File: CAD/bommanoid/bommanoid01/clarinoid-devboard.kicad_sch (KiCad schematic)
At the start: 144 parts, among them IC1 PCA9554APW,118, J1 AudioOut, J10 MIDI IN, J11 MIDI OUT, J12 SSD1306, J13 captouch 3x3x1 header B, J14 captouch4x4x2 headerA, J15 captouch4x4x2 header B, J16 captouch4x4x2, J17 captouch4x4x3 headerA, J18 captouch4x4x3 header B, J19 captouch4x4x.5 headerA, J2 XKB_U262-16XN-4BVC11 USB-C re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, J20 CapTouchSlider_3x3x1, J21 captouch4x4x.5 header B, J22 captouch4x4x3, J23 captouch4x4x.5, J24 captouch5x5x1 headerA, J25 captouch5x5x1 header B, J26 captouch4x4x1 headerA, J27 captouch4x4x1 header B, J28 captouch5x5x1, J29 captouch4x4x1, J31 4p, J32 header_power tap, J43 Conn_01x20, J44 Conn_01x08, J45 female 1x6, J5 header_i2c, J52 female 1x6, J53 female 1x6, J6 female 1x6, J8 female 1x4, J9 captouch 3x3x1 headerA, SW2 SW_Push, SW3 SW_Push, SW4 SW_Push, SW5 SW_Push, SW7 RotaryEncoder_Switch_ABC12, U1 PCM5102A, U10 captouch4x4x2 graphic, U11 captouch4x4x3 graphic, U12 ssd1306_graphic, U13 captouch4x4x.5 graphic, U14 captouch5x5x1 graphic, U15 captouch4x4x1 graphic, U16 power template, U20 mb1, U21 mb1, U22 mb1, U23 mb1, U24 mb1, U25 mb1, U26 mb1, U27 mb1, U28 mb1, U29 mb1, U30 mb1, U31 mb1, U32 mb1, U33 mb1, U34 mb1, U35 mb1, U36 mb1, U37 mb1, U38 WS2812, U4 captouch board template, U44 processor board template, U48 mb1, U49 mb1, U50 mb1, U51 mb1, U52 mb1, U53 mb1, U54 mb1, U55 mb1, U56 mb1, U57 mb1, U58 mb1, U59 mb1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

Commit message: bomma design progress
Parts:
- removed C10, C11, C3, C5: 10uF, Capacitor_SMD:C_0805_2012Metric, symbol Device:C
- removed C12, C7, C8, C9: 2.2uF, Capacitor_SMD:C_0805_2012Metric, symbol Device:C
- removed C13, C14, C23, C27, C4, C6: 0.1uF, Capacitor_SMD:C_0805_2012Metric, symbol Device:C
- removed C17, C20, C21, C22: 22uF, Capacitor_SMD:C_0805_2012Metric, symbol Device:C
- removed D5, D7: blue, LED_SMD:LED_0603_1608Metric, symbol Device:LED
- removed D6: 1N4148WS, Diode_SMD:D_SOD-323, symbol Device:D
- removed D8, D9: green, LED_SMD:LED_0603_1608Metric, symbol Device:LED
- removed H1: MountingHole, clarinoid2:MountingHole_3.2mm_M3_Pad_SQUARE, symbol Mechanical:MountingHole_Pad
- removed H13, H14, H15: MountingHole, MountingHole:MountingHole_3.2mm_M3, symbol Mechanical:MountingHole
- removed H2, H3, H5: MountingHole, MountingHole:MountingHole_3.2mm_M3_Pad_Via, symbol Mechanical:MountingHole_Pad
- removed IC1: PCA9554APW,118, SamacSys_Parts:SOP65P640X110-16N, symbol SamacSys_Parts:PCA9554APW,118
- removed J1: AudioOut, clarinoid2:SWITCHCRAFT_35RAPC4BV4_OvalHoles, symbol clarinoid2:Switchcraft 35RAPC4BV4
- removed J10: MIDI IN, clarinoid2:SWITCHCRAFT_35RAPC4BV4_OvalHoles, symbol clarinoid2:Switchcraft 35RAPC4BV4
- removed J11: MIDI OUT, clarinoid2:SWITCHCRAFT_35RAPC4BV4_OvalHoles, symbol clarinoid2:Switchcraft 35RAPC4BV4
- removed J12: SSD1306, Connector_PinSocket_2.54mm:PinSocket_1x07_P2.54mm_Vertical, symbol clarinoid2:SSD1306
- removed J13: captouch 3x3x1 header B, Connector_PinHeader_2.54mm:PinHeader_1x06_P2.54mm_Vertical, symbol Connector_Generic:Conn_01x06
- removed J14: captouch4x4x2 headerA, Connector_PinHeader_2.54mm:PinHeader_1x06_P2.54mm_Vertical, symbol Connector_Generic:Conn_01x06
- removed J15: captouch4x4x2 header B, Connector_PinHeader_2.54mm:PinHeader_1x06_P2.54mm_Vertical, symbol Connector_Generic:Conn_01x06
- removed J16: captouch4x4x2, CapTouchSliders:CaptouchSlider_Masked_H4x4_A2.0mm_x12, symbol Connector_Generic:Conn_01x12
- removed J17: captouch4x4x3 headerA, Connector_PinHeader_2.54mm:PinHeader_1x06_P2.54mm_Vertical, symbol Connector_Generic:Conn_01x06
- removed J18: captouch4x4x3 header B, Connector_PinHeader_2.54mm:PinHeader_1x06_P2.54mm_Vertical, symbol Connector_Generic:Conn_01x06
- removed J19: captouch4x4x.5 headerA, Connector_PinHeader_2.54mm:PinHeader_1x06_P2.54mm_Vertical, symbol Connector_Generic:Conn_01x06
- removed J2: XKB_U262-16XN-4BVC11 USB-C recept, clarinoid2:USB_C_Receptacle_XKB_U262-16XN-4BVC11, symbol clarinoid2:USB_C_Plug_USB2.0
- removed J20: CapTouchSlider_3x3x1, CapTouchSliders:CaptouchSlider_Masked_H3x3_A1.0mm_x12, symbol Connector_Generic:Conn_01x12
- removed J21: captouch4x4x.5 header B, Connector_PinHeader_2.54mm:PinHeader_1x06_P2.54mm_Vertical, symbol Connector_Generic:Conn_01x06
- removed J22: captouch4x4x3, CapTouchSliders:CaptouchSlider_Masked_H4x4_A3.0mm_x12, symbol Connector_Generic:Conn_01x12
- removed J23: captouch4x4x.5, CapTouchSliders:CaptouchSlider_Masked_H4x4_A0.5mm_x12, symbol Connector_Generic:Conn_01x12
- removed J24: captouch5x5x1 headerA, Connector_PinHeader_2.54mm:PinHeader_1x06_P2.54mm_Vertical, symbol Connector_Generic:Conn_01x06
- removed J25: captouch5x5x1 header B, Connector_PinHeader_2.54mm:PinHeader_1x06_P2.54mm_Vertical, symbol Connector_Generic:Conn_01x06
- removed J26: captouch4x4x1 headerA, Connector_PinHeader_2.54mm:PinHeader_1x06_P2.54mm_Vertical, symbol Connector_Generic:Conn_01x06
- removed J27: captouch4x4x1 header B, Connector_PinHeader_2.54mm:PinHeader_1x06_P2.54mm_Vertical, symbol Connector_Generic:Conn_01x06
- removed J28: captouch5x5x1, CapTouchSliders:CaptouchSlider_Masked_H5x5_A1.0mm_x12, symbol Connector_Generic:Conn_01x12
- removed J29: captouch4x4x1, CapTouchSliders:CaptouchSlider_Masked_H4x4_A1.0mm_x12, symbol Connector_Generic:Conn_01x12
- removed J31: 4p, Connector_PinSocket_2.54mm:PinSocket_1x04_P2.54mm_Vertical, symbol Connector_Generic:Conn_01x04
- removed J32: header_power tap, Connector_PinSocket_2.54mm:PinSocket_1x02_P2.54mm_Vertical, symbol Connector_Generic:Conn_01x02
- removed J43: Conn_01x20, Connector_PinSocket_2.54mm:PinSocket_1x20_P2.54mm_Vertical, symbol Connector_Generic:Conn_01x20
- removed J44: Conn_01x08, Connector_PinSocket_2.54mm:PinSocket_1x08_P2.54mm_Vertical, symbol Connector_Generic:Conn_01x08
- removed J45, J52, J53, J6: female 1x6, Connector_PinSocket_2.54mm:PinSocket_1x06_P2.54mm_Vertical, symbol Connector_Generic:Conn_01x06
- removed J5: header_i2c, Connector_PinSocket_2.54mm:PinSocket_1x04_P2.54mm_Vertical, symbol Connector_Generic:Conn_01x04
- removed J8: female 1x4, Connector_PinSocket_2.54mm:PinSocket_1x04_P2.54mm_Vertical, symbol Connector_Generic:Conn_01x04
- removed J9: captouch 3x3x1 headerA, Connector_PinHeader_2.54mm:PinHeader_1x06_P2.54mm_Vertical, symbol Connector_Generic:Conn_01x06
- removed NT1: NetTie_2, NetTie:NetTie-2_SMD_Pad0.5mm, symbol Device:NetTie_2
- removed R1, R2, R3: 22R, Resistor_SMD:R_1206_3216Metric, symbol Device:R
- removed R13: PTR902-2020K-A103, SamacSys_Parts:PTR902-2020K-A103, symbol SamacSys_Parts:PTR902-2020K-A103
- removed R19: 220R, Resistor_SMD:R_1206_3216Metric, symbol Device:R
- removed R20, R21: 47R, Resistor_SMD:R_1206_3216Metric, symbol Device:R
- removed R22, R34, R35, R36, R37, R5, R6: 470R, Resistor_SMD:R_1206_3216Metric, symbol Device:R
- removed R40, R41: 4.7k, Resistor_SMD:R_1206_3216Metric, symbol Device:R
- removed R7, R8: 5.1k, Resistor_SMD:R_1206_3216Metric, symbol Device:R
- removed SW2, SW3, SW4, SW5: SW_Push, SamacSys_Parts:B3F-4055, symbol Switch:SW_Push
- removed SW7: RotaryEncoder_Switch_ABC12, clarinoid2:Bourns_ENC_PEC11R-4215F-S0024, symbol clarinoid2:RotaryEncoder_Switch_ABC12
- removed TP3: AGND, TestPoint:TestPoint_THTPad_D2.0mm_Drill1.0mm, symbol Connector:TestPoint
- removed TP6: D3v3, TestPoint:TestPoint_THTPad_D2.0mm_Drill1.0mm, symbol Connector:TestPoint
- removed TP8: A3v3, TestPoint:TestPoint_THTPad_D2.0mm_Drill1.0mm, symbol Connector:TestPoint
- removed U1: PCM5102A, Package_SO:TSSOP-20_4.4x6.5mm_P0.65mm, symbol clarinoid2:PCM5102
- removed U10: captouch4x4x2 graphic, CapTouchSliders:captouch dev board subboard template, symbol clarinoid2:Placeholder
- removed U11: captouch4x4x3 graphic, CapTouchSliders:captouch dev board subboard template, symbol clarinoid2:Placeholder
- removed U12: ssd1306_graphic, clarinoid2:SSD1306_128x64_approximate, symbol clarinoid2:Placeholder
- removed U13: captouch4x4x.5 graphic, CapTouchSliders:captouch dev board subboard template, symbol clarinoid2:Placeholder
- removed U14: captouch5x5x1 graphic, CapTouchSliders:captouch dev board subboard template, symbol clarinoid2:Placeholder
- removed U15: captouch4x4x1 graphic, CapTouchSliders:captouch dev board subboard template, symbol clarinoid2:Placeholder
- removed U16: power template, clarinoid2:dev board power board template, symbol clarinoid2:Placeholder
- removed U20, U21, U22, U23, U24, U25, U26, U27, U28, U29, U30, U31, U32, U33, U34, U35, U36, U37, U48, U49, U50, U51, U52, U53, U54, U55, U56, U57, U58, U59, U60, U61, U62, U63, U64, U65, U66, U67, U68: mb1, clarinoid2:mouse-bite-2mm-slot, symbol clarinoid2:Placeholder
- removed U38: WS2812, Connector_PinSocket_2.54mm:PinSocket_1x03_P2.54mm_Vertical, symbol clarinoid2:WS2812
- removed U4: captouch board template, clarinoid2:dev board captouch board template, symbol clarinoid2:Placeholder
- removed U44: processor board template, clarinoid2:dev board processor subboard template, symbol clarinoid2:Placeholder
- removed U7: TLV75733PDBV, Package_TO_SOT_SMD:SOT-23-5, symbol Regulator_Linear:TLV75533PDBV
- removed U8: 6N138, Package_DIP:DIP-8_W7.62mm, symbol Isolator:6N138
- removed U9: captouch3x3x1 graphic, CapTouchSliders:captouch dev board subboard template, symbol clarinoid2:Placeholder
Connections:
- no-connect marks 14 -> 0
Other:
- removed sheet captouch_capsense
- removed sheet captouch_mpr121
- removed sheet power_battery
- removed sheet power_header
- removed sheet power_usb
- removed sheet processor_mm
- removed sheet processor_t4
- added sheet bell (bell.kicad_sch)
- added sheet bommanoid_batt_bottom (bommanoid_batt_bottom.kicad_sch)
- added sheet bommanoid_batt_top (bommanoid_batt_top.kicad_sch)
- added sheet bommanoid_main_bottom (bommanoid_main_bottom.kicad_sch)
- added sheet bommanoid_main_top (bommanoid_main_top.kicad_sch)
- added sheet cab (cab.kicad_sch)
- note removed: "DAC - PCM5102A"
- note removed: "HEADERs"
- note removed: "MIDI IN"
- note removed: "MIDI OUT"
- note removed: "PCA9554APW,118 0x38"
- note removed: "USB-C input"
- note removed: "WS2812"
- note removed: "encoder"
- note removed: "smt leds"
- note removed: "todo: x length match x silkscreen, drc, erc x switch footprints x exclude backside headers from BOM as needed - JLCPCB part numbers for headers"

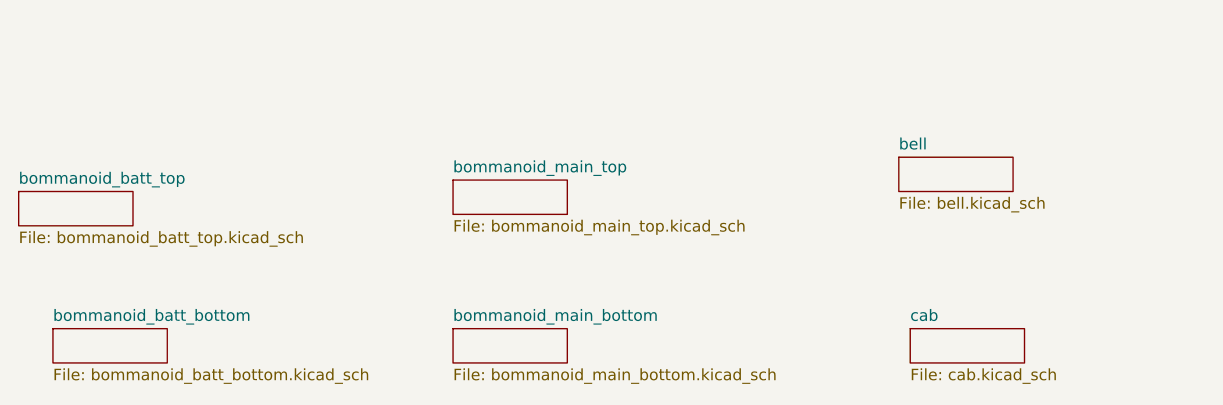
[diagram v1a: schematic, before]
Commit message: progress on bommanoid pcb design adding some winisd simulations
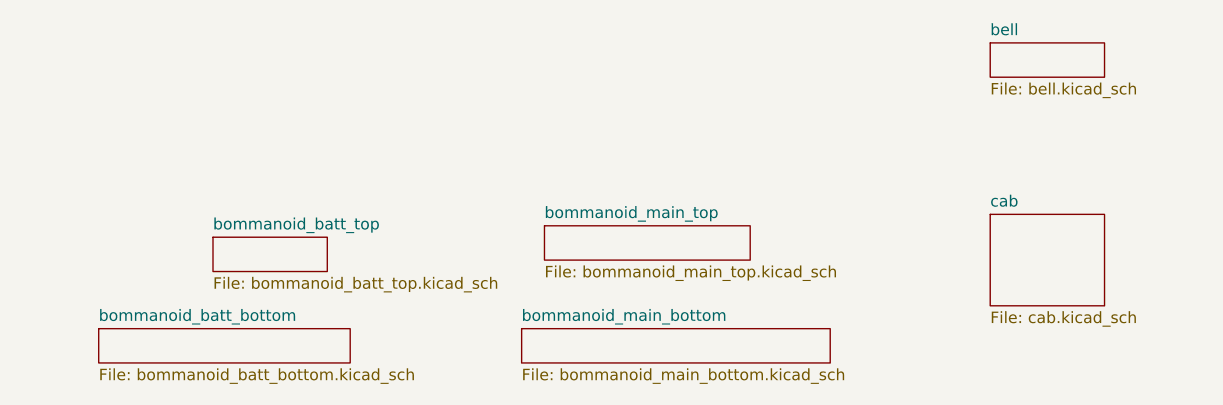
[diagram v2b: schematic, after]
